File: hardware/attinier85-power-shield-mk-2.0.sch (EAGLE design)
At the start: 6 parts, among them IC1 MC34063DIP, U1 ATTINIEST85_SHIELDV2

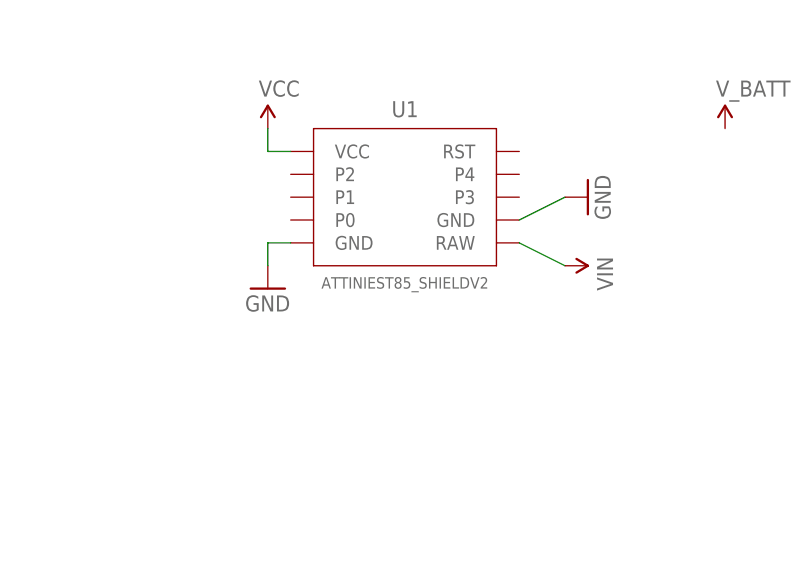
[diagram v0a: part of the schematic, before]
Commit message: renaming parts
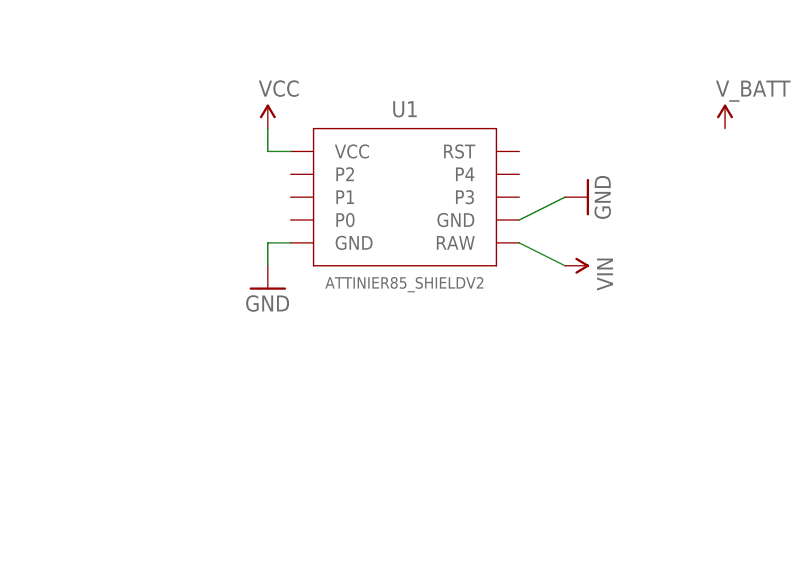
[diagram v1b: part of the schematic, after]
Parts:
- U1: value ATTINIEST85_SHIELDV2 -> ATTINIER85_SHIELDV2; device A_butts:ATTINIEST85_SHIELDV2 -> A_butts:ATTINIER85_SHIELDV2
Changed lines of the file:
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@@
 <parts>
 <part name="FRAME1" library="A_butts" deviceset="FRAME-LETTER" device="NO_PACKAGE"/>
-<part name="U1" library="A_butts" deviceset="ATTINIEST85_SHIELD" device="V2"/>
+<part name="U1" library="A_butts" deviceset="ATTINIER85_SHIELD" device="V2"/>
 <part name="SUPPLY1" library="A_butts" deviceset="VCC" device=""/>
 <part name="SUPPLY2" library="A_butts" deviceset="V_BATT" device=""/>
